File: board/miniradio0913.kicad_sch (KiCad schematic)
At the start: 28 parts, among them J1 AudioJack3, J2 Conn_01x03_Socket, J3 USB_B_Micro, Q2 Q_PMOS_GSD, SW1 SW_Push, SW2 SW_Push, SW3 SW_Push, U1 CH32V003JxMx, U2 KT0913, U3 AQM0802, Y2 Crystal_GND2

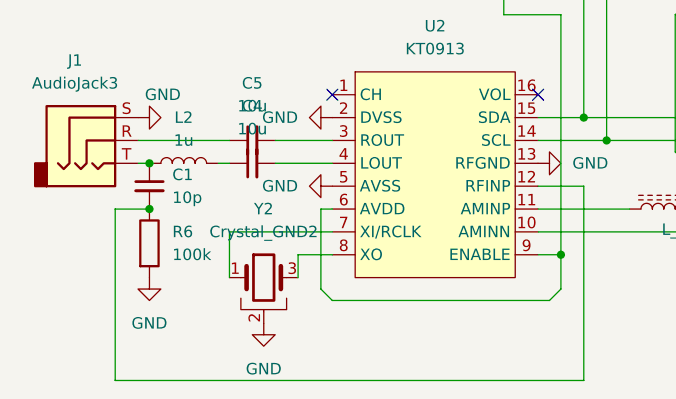
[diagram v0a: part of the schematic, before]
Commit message: fix(board): crystal
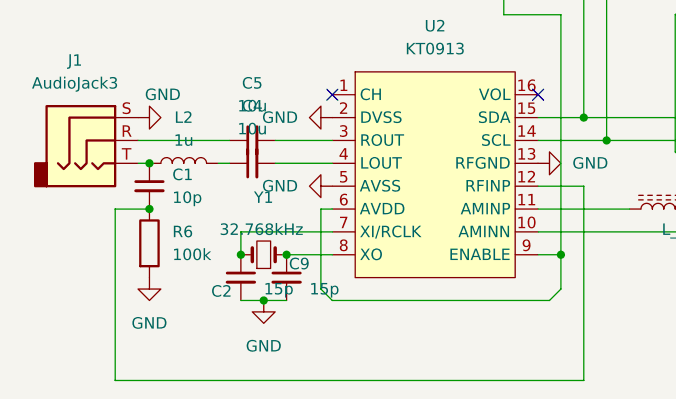
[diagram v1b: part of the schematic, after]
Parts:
- removed Y2: Crystal_GND2, Library:SMD_Crystal_Murata, symbol Device:Crystal_GND2
- added C2, C9: 15p, Capacitor_SMD:C_0603_1608Metric, symbol Device:C_Small
- added Y1: 32.768kHz, Crystal:Crystal_SMD_3215-2Pin_3.2x1.5mm, symbol Device:Crystal_Small
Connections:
- net GND: now also C2.2, C9.2
- net at U2.7 (XI/RCLK): now also C2.1, Y1.1
- net at U2.8 (XO): now also C9.1, Y1.2
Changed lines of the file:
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@@
 	)
 	(junction
+		(at 109.22 120.65)
+		(diameter 0)
+		(color 0 0 0 0)
+	)
+	(junction
 		(at 104.14 48.26)
 		(diameter 0)
@@
 	)
 	(junction
+		(at 111.76 115.57)
+		(diameter 0)
+		(color 0 0 0 0)
+	)
+	(junction
 		(at 196.85 102.87)
 		(diameter 0)
@@
 	)
 	(junction
+		(at 106.68 115.57)
+		(diameter 0)
+		(color 0 0 0 0)
+	)
+	(junction
 		(at 147.32 102.87)
 		(diameter 0)
@@
 	(wire
 		(pts
-			(xy 113.03 115.57) (xy 113.03 118.11)
-		)
-		(stroke
-			(width 0)
-			(type default)
-		)
-	)
-	(wire
-		(pts
 			(xy 152.4 67.31) (xy 158.75 67.31)
 		)
@@
 	(wire
 		(pts
-			(xy 105.41 113.03) (xy 105.41 118.11)
-		)
-		(stroke
-			(width 0)
-			(type default)
-		)
-	)
-	(wire
-		(pts
 			(xy 104.14 49.53) (xy 104.14 48.26)
 		)
@@
 	(wire
 		(pts
-			(xy 105.41 113.03) (xy 116.84 113.03)
+			(xy 106.68 113.03) (xy 116.84 113.03)
 		)
 		(stroke
@@
 	(wire
 		(pts
+			(xy 111.76 115.57) (xy 116.84 115.57)
+		)
+		(stroke
+			(width 0)
+			(type default)
+		)
+	)
+	(wire
+		(pts
 			(xy 156.21 105.41) (xy 154.94 104.14)
 		)
@@
 	(wire
 		(pts
-			(xy 113.03 115.57) (xy 116.84 115.57)
+			(xy 104.14 105.41) (xy 105.41 105.41)
 		)
 		(stroke
@@
 	(wire
 		(pts
-			(xy 104.14 105.41) (xy 105.41 105.41)
+			(xy 115.57 110.49) (xy 116.84 110.49)
 		)
 		(stroke
@@
 	(wire
 		(pts
-			(xy 115.57 110.49) (xy 116.84 110.49)
+			(xy 109.22 120.65) (xy 111.76 120.65)
+		)
+		(stroke
+			(width 0)
+			(type default)
+		)
+	)
+	(wire
+		(pts
+			(xy 106.68 113.03) (xy 106.68 115.57)
 		)
 		(stroke
@@
 	(wire
 		(pts
+			(xy 106.68 120.65) (xy 109.22 120.65)
+		)
+		(stroke
+			(width 0)
+			(type default)
+		)
+	)
+	(wire
+		(pts
 			(xy 154.94 88.9) (xy 156.21 87.63)
 		)
@@
 	)
 	(symbol
-		(lib_id "Device:Crystal_GND2")
-		(at 109.22 118.11 0)
-		(unit 1)
-		(exclude_from_sim no)
-		(in_bom yes)
-		(on_board yes)
-		(dnp no)
-		(fields_autoplaced yes)
-		(property "Reference" "Y2"
-			(at 109.22 110.49 0)
-			(effects
-				(font
-					(size 1.27 1.27)
-				)
-			)
-		)
-		(property "Value" "Crystal_GND2"
-			(at 109.22 113.03 0)
-			(effects
-				(font
-					(size 1.27 1.27)
-				)
-			)
-		)
-		(property "Footprint" "Library:SMD_Crystal_Murata"
-			(at 109.22 118.11 0)
-			(effects
-				(font
-					(size 1.27 1.27)
-				)
-				(hide yes)
-			)
-		)
-		(property "Datasheet" "~"
-			(at 109.22 118.11 0)
-			(effects
-				(font
-					(size 1.27 1.27)
-				)
-				(hide yes)
-			)
-		)
-		(property "Description" "Three pin crystal, GND on pin 2"
-			(at 109.22 118.11 0)
-			(effects
-				(font
-					(size 1.27 1.27)
-				)
-				(hide yes)
-			)
-		)
-		(pin "2"
-		)
-		(pin "1"
-		)
-		(pin "3"
-		)
-		(instances
-			(project ""
-				(path "/b7ea65bb-5637-4a68-8262-64ffd95ecdcf"
-					(reference "Y2")
-					(unit 1)
-				)
-			)
-		)
-	)
-	(symbol
 		(lib_id "Switch:SW_Push")
 		(at 201.93 102.87 0)
@@
 	)
 	(symbol
+		(lib_id "Device:Crystal_Small")
+		(at 109.22 115.57 0)
+		(unit 1)
+		(exclude_from_sim no)
+		(in_bom yes)
+		(on_board yes)
+		(dnp no)
+		(property "Reference" "Y1"
+			(at 109.22 109.22 0)
+			(effects
+				(font
+					(size 1.27 1.27)
+				)
+			)
+		)
+		(property "Value" "32.768kHz"
+			(at 108.966 112.776 0)
+			(effects
+				(font
+					(size 1.27 1.27)
+				)
+			)
+		)
+		(property "Footprint" "Crystal:Crystal_SMD_3215-2Pin_3.2x1.5mm"
+			(at 109.22 115.57 0)
+			(effects
+				(font
+					(size 1.27 1.27)
+				)
+				(hide yes)
+			)
+		)
+		(property "Datasheet" "~"
+			(at 109.22 115.57 0)
+			(effects
+				(font
+					(size 1.27 1.27)
+				)
+				(hide yes)
+			)
+		)
+		(property "Description" "Two pin crystal, small symbol"
+			(at 109.22 115.57 0)
+			(effects
+				(font
+					(size 1.27 1.27)
+				)
+				(hide yes)
+			)
+		)
+		(pin "2"
+		)
+		(pin "1"
+		)
+		(instances
+			(project ""
+				(path "/b7ea65bb-5637-4a68-8262-64ffd95ecdcf"
+					(reference "Y1")
+					(unit 1)
+				)
+			)
+		)
+	)
+	(symbol
+		(lib_id "Device:C_Small")
+		(at 106.68 118.11 0)
+		(unit 1)
+		(exclude_from_sim no)
+		(in_bom yes)
+		(on_board yes)
+		(dnp no)
+		(property "Reference" "C2"
+			(at 103.378 119.6402 0)
+			(effects
+				(font
+					(size 1.27 1.27)
+				)
+				(justify left)
+			)
+		)
+		(property "Value" "15p"
+			(at 109.22 119.3862 0)
+			(effects
+				(font
+					(size 1.27 1.27)
+				)
+				(justify left)
+			)
+		)
+		(property "Footprint" "Capacitor_SMD:C_0603_1608Metric"
+			(at 106.68 118.11 0)
+			(effects
+				(font
+					(size 1.27 1.27)
+				)
+				(hide yes)
+			)
+		)
+		(property "Datasheet" "~"
+			(at 106.68 118.11 0)
+			(effects
+				(font
+					(size 1.27 1.27)
+				)
+				(hide yes)
+			)
+		)
+		(property "Description" "Unpolarized capacitor, small symbol"
+			(at 106.68 118.11 0)
+			(effects
+				(font
+					(size 1.27 1.27)
+				)
+				(hide yes)
+			)
+		)
+		(pin "2"
+		)
+		(pin "1"
+		)
+		(instances
+			(project ""
+				(path "/b7ea65bb-5637-4a68-8262-64ffd95ecdcf"
+					(reference "C2")
+					(unit 1)
+				)
+			)
+		)
+	)
+	(symbol
 		(lib_id "Device:Battery")
 		(at 109.22 59.69 0)
@@
 	)
 	(symbol
+		(lib_id "Device:C_Small")
+		(at 111.76 118.11 0)
+		(unit 1)
+		(exclude_from_sim no)
+		(in_bom yes)
+		(on_board yes)
+		(dnp no)
+		(property "Reference" "C9"
+			(at 112.014 116.5922 0)
+			(effects
+				(font
+					(size 1.27 1.27)
+				)
+				(justify left)
+			)
+		)
+		(property "Value" "15p"
+			(at 114.3 119.3862 0)
+			(effects
+				(font
+					(size 1.27 1.27)
+				)
+				(justify left)
+			)
+		)
+		(property "Footprint" "Capacitor_SMD:C_0603_1608Metric"
+			(at 111.76 118.11 0)
+			(effects
+				(font
+					(size 1.27 1.27)
+				)
+				(hide yes)
+			)
+		)
+		(property "Datasheet" "~"
+			(at 111.76 118.11 0)
+			(effects
+				(font
+					(size 1.27 1.27)
+				)
+				(hide yes)
+			)
+		)
+		(property "Description" "Unpolarized capacitor, small symbol"
+			(at 111.76 118.11 0)
+			(effects
+				(font
+					(size 1.27 1.27)
+				)
+				(hide yes)
+			)
+		)
+		(pin "2"
+		)
+		(pin "1"
+		)
+		(instances
+			(project ""
+				(path "/b7ea65bb-5637-4a68-8262-64ffd95ecdcf"
+					(reference "C9")
+					(unit 1)
+				)
+			)
+		)
+	)
+	(symbol
 		(lib_id "Device:R")
 		(at 215.9 109.22 0)
@@
 	(symbol
 		(lib_id "power:GND")
-		(at 109.22 123.19 0)
+		(at 109.22 120.65 0)
 		(unit 1)
 		(exclude_from_sim no)
@@
 		(fields_autoplaced yes)
 		(property "Reference" "#PWR08"
-			(at 109.22 129.54 0)
+			(at 109.22 127 0)
 			(effects
 				(font
@@
 		)
 		(property "Value" "GND"
-			(at 109.22 128.27 0)
+			(at 109.22 125.73 0)
 			(effects
 				(font
@@
 		)
 		(property "Footprint" ""
-			(at 109.22 123.19 0)
+			(at 109.22 120.65 0)
 			(effects
 				(font
@@
 		)
 		(property "Datasheet" ""
-			(at 109.22 123.19 0)
+			(at 109.22 120.65 0)
 			(effects
 				(font
@@
 		)
 		(property "Description" "Power symbol creates a global label with name \"GND\" , ground"
-			(at 109.22 123.19 0)
+			(at 109.22 120.65 0)
 			(effects
 				(font

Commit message: board: update
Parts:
- removed BT2: Battery, Library:CH25-2032LF, symbol Device:Battery
- removed D1: D_Small, Diode_SMD:D_0603_1608Metric, symbol Device:D_Small
- removed J3: USB_B_Micro, Library:usb_microb_power_MRUSB-2B-D14NI-S306, symbol Connector:USB_B_Micro
- removed R1: R, Resistor_SMD:R_0603_1608Metric, symbol Device:R
- removed R5: 10k, Resistor_SMD:R_0603_1608Metric, symbol Device:R
- BT1: footprint Battery:BatteryHolder_Keystone_1060_1x2032 -> Library:BH-521_2xN
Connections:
- net VDD: now also BT1.1 (+), Q2.2 (S); no longer Q2.3 (D)
- net at C6.1, C8.1, U2.6 (AVDD)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: now also Q2.3 (D); no longer Q2.2 (S)
- no-connect marks 6 -> 3
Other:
- moved on the sheet: Q2

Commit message: board: update
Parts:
- added C10: 0.1u, Capacitor_SMD:C_0603_1608Metric, symbol Device:C_Small
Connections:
- net GND: now also C10.1
- net VDD: now also C10.2
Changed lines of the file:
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@@
 	)
 	(junction
+		(at 176.53 95.25)
+		(diameter 0)
+		(color 0 0 0 0)
+	)
+	(junction
 		(at 144.78 100.33)
 		(diameter 0)
@@
 	(wire
 		(pts
+			(xy 173.99 95.25) (xy 176.53 95.25)
+		)
+		(stroke
+			(width 0)
+			(type default)
+		)
+	)
+	(wire
+		(pts
 			(xy 154.94 88.9) (xy 154.94 104.14)
 		)
@@
 	)
 	(symbol
+		(lib_id "power:GND")
+		(at 168.91 95.25 270)
+		(unit 1)
+		(exclude_from_sim no)
+		(in_bom yes)
+		(on_board yes)
+		(dnp no)
+		(fields_autoplaced yes)
+		(property "Reference" "#PWR06"
+			(at 162.56 95.25 0)
+			(effects
+				(font
+					(size 1.27 1.27)
+				)
+				(hide yes)
+			)
+		)
+		(property "Value" "GND"
+			(at 165.1 95.2499 90)
+			(effects
+				(font
+					(size 1.27 1.27)
+				)
+				(justify right)
+			)
+		)
+		(property "Footprint" ""
+			(at 168.91 95.25 0)
+			(effects
+				(font
+					(size 1.27 1.27)
+				)
+				(hide yes)
+			)
+		)
+		(property "Datasheet" ""
+			(at 168.91 95.25 0)
+			(effects
+				(font
+					(size 1.27 1.27)
+				)
+				(hide yes)
+			)
+		)
+		(property "Description" "Power symbol creates a global label with name \"GND\" , ground"
+			(at 168.91 95.25 0)
+			(effects
+				(font
+					(size 1.27 1.27)
+				)
+				(hide yes)
+			)
+		)
+		(pin "1"
+		)
+		(instances
+			(project ""
+				(path "/b7ea65bb-5637-4a68-8262-64ffd95ecdcf"
+					(reference "#PWR06")
+					(unit 1)
+				)
+			)
+		)
+	)
+	(symbol
 		(lib_id "Device:C_Small")
 		(at 151.13 68.58 0)
@@
 					(unit 1)
 				)
+			)
+		)
+	)
+	(symbol
+		(lib_id "Device:C_Small")
+		(at 171.45 95.25 90)
+		(unit 1)
+		(exclude_from_sim no)
+		(in_bom yes)
+		(on_board yes)
+		(dnp no)
+		(property "Reference" "C10"
+			(at 168.402 90.424 90)
+			(effects
+				(font
+					(size 1.27 1.27)
+				)
+			)
+		)
+		(property "Value" "0.1u"
+			(at 168.402 92.964 90)
+			(effects
+				(font
+					(size 1.27 1.27)
+				)
+			)
+		)
+		(property "Footprint" "Capacitor_SMD:C_0603_1608Metric"
+			(at 171.45 95.25 0)
+			(effects
+				(font
+					(size 1.27 1.27)
+				)
+				(hide yes)
+			)
+		)
+		(property "Datasheet" "~"
+			(at 171.45 95.25 0)
+			(effects
+				(font
+					(size 1.27 1.27)
+				)
+				(hide yes)
+			)
+		)
+		(property "Description" "Unpolarized capacitor, small symbol"
+			(at 171.45 95.25 0)
+			(effects
+				(font
+					(size 1.27 1.27)
+				)
+				(hide yes)
+			)
+		)
+		(pin "2"
+		)
+		(pin "1"
+		)
+		(instances
+			(project ""
+				(path "/b7ea65bb-5637-4a68-8262-64ffd95ecdcf"
+					(reference "C10")
+					(unit 1)
+				)

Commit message: board: renumber parts
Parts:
- renumbered C3 to C1, C9 to C10, C6 to C2, C7 to C3, C8 to C4, C10 to C5, C5 to C6, C4 to C7, C1 to C8, C2 to C9, J2 to J1, J1 to J2, L2 to L1, L1 to L2, Q2 to Q1, R3 to R1, R6 to R3, SW2 to SW1, SW1 to SW2, U3 to U1, U1 to U2, U2 to U3
